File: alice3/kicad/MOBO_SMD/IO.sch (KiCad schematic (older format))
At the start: 36 parts, among them CON1 MicroSD, P2 USB_OTG, P3 UART1, SW2 SOFT RESET, U5 STM32F415RG, Y2 16MHz, Y3 32.768KHz

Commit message: Fix up various small things.
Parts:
- added C?: 1µ, Capacitors_SMD:C_0805, symbol C_Small
- added C?: 4.7µ, Capacitors_SMD:C_0805, symbol C_Small
- added F?: F_Small, symbol F_Small
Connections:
- wire segments 108 -> 148
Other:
- moved on the sheet: C2, C8, JP1, R3, R4

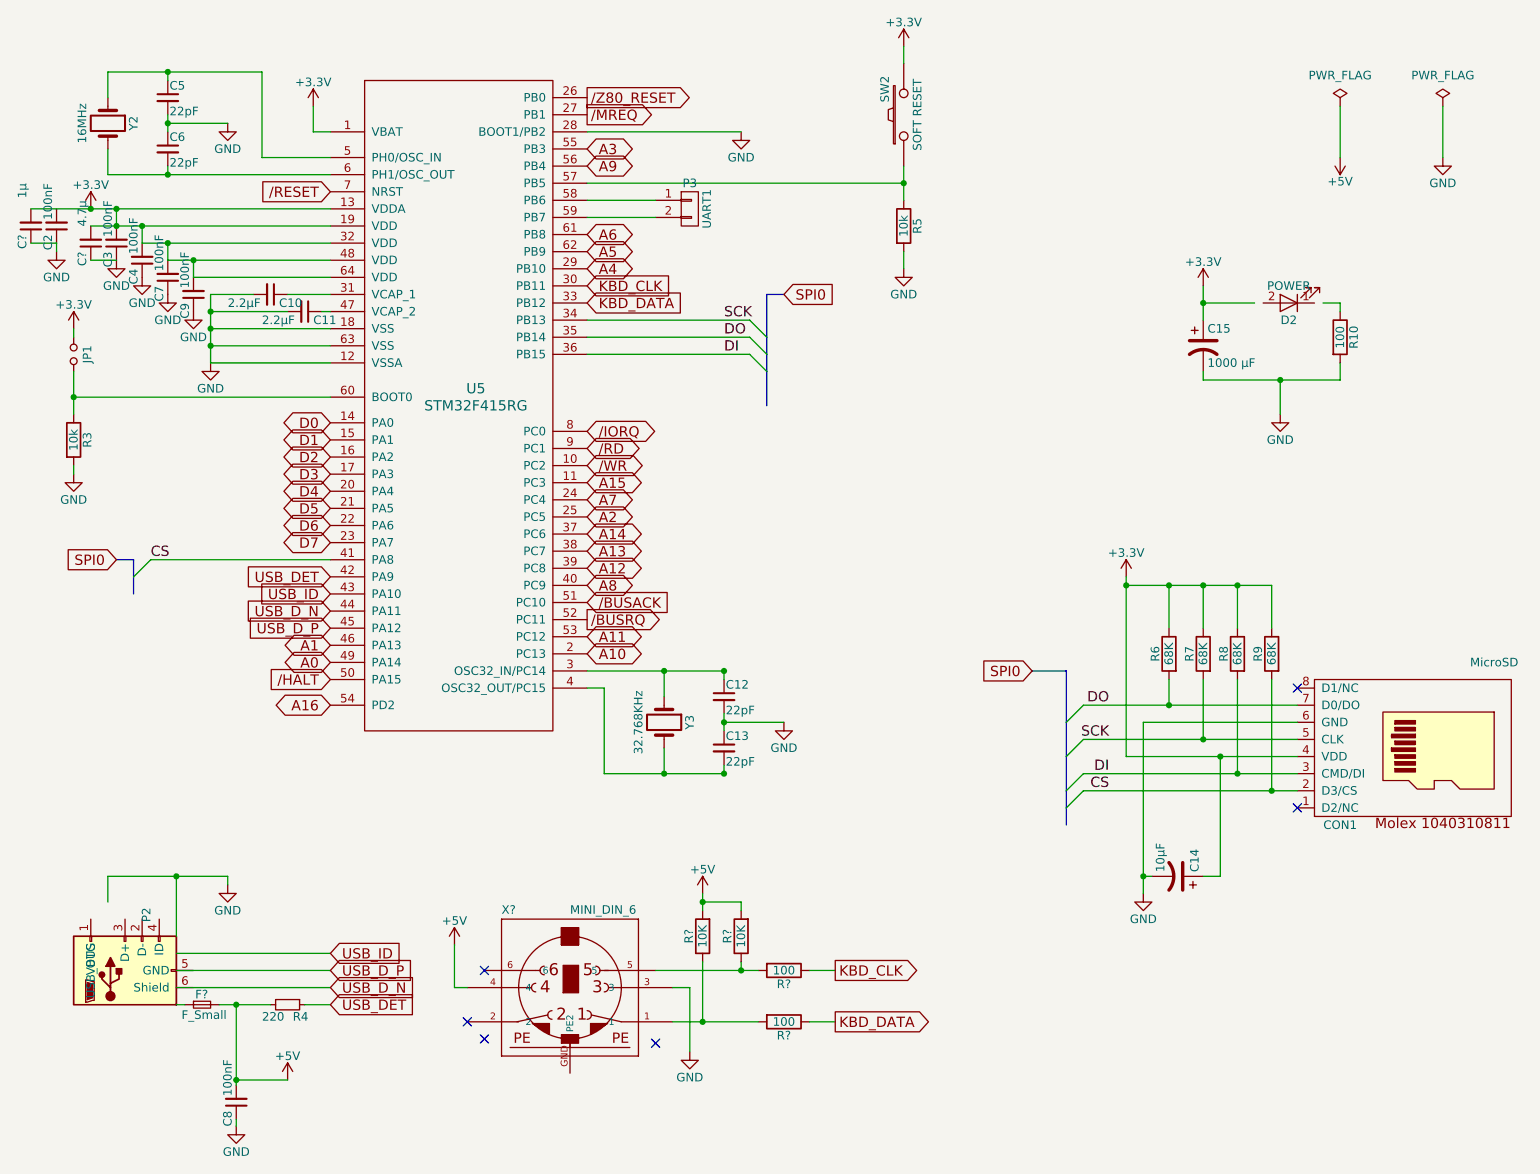
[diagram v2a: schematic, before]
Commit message: Assign part names.
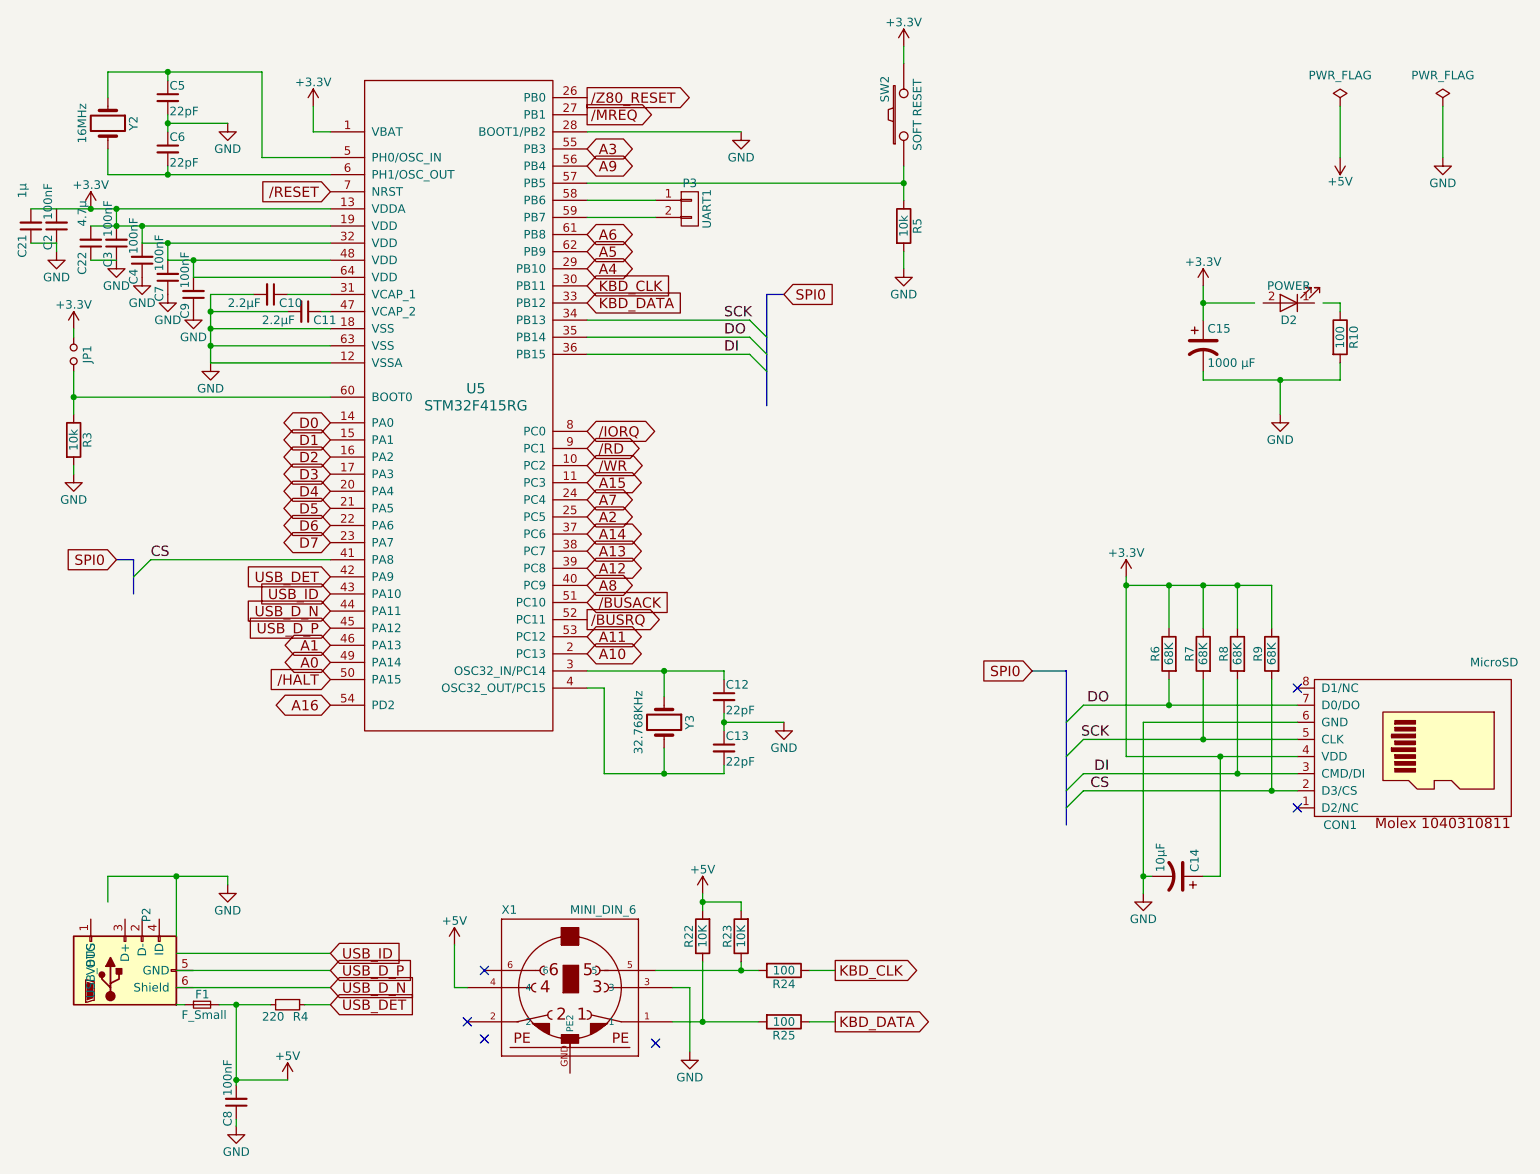
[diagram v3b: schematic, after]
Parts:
- gave numbers to parts that had none: 8
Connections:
- wire segments 148 -> 113

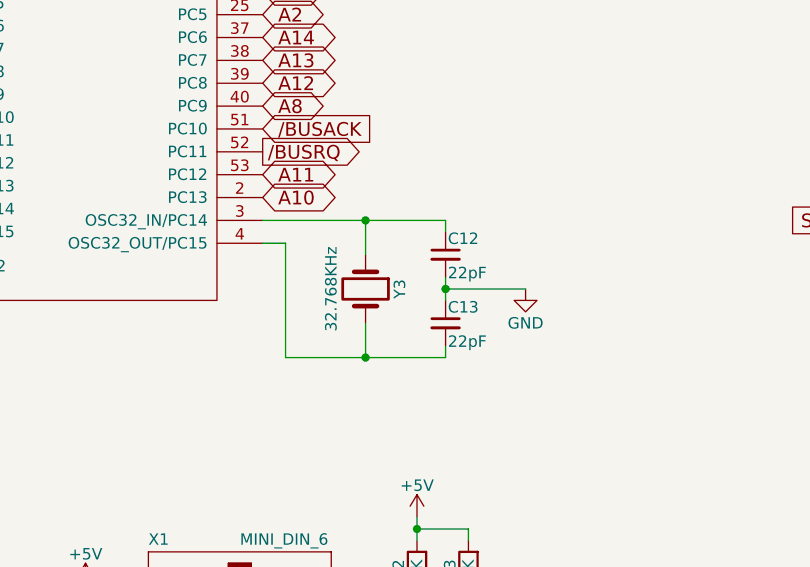
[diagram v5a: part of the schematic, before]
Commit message: Add PROP_READY line; add A17 to ARM.
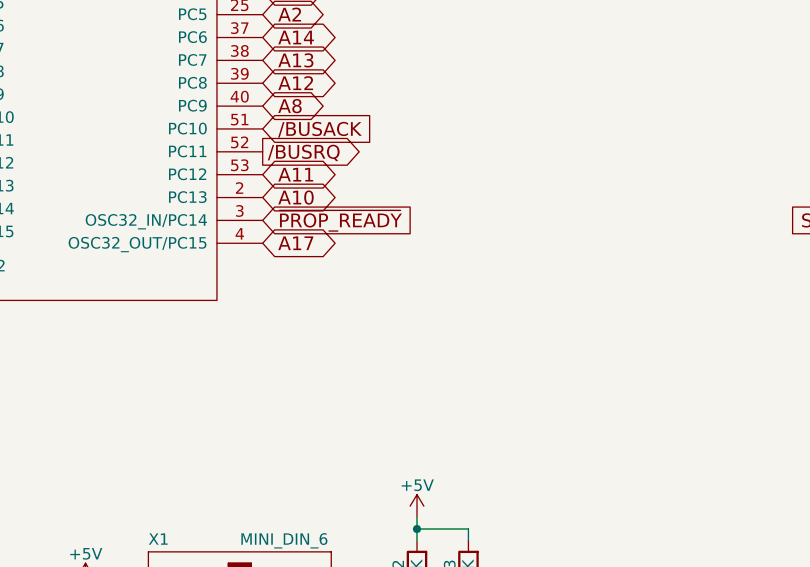
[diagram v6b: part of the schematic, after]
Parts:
- removed C12, C13: 22pF, Capacitors_SMD:C_0805, symbol C_Small
- removed Y3: 32.768KHz, Resistors_SMD:R_0805, symbol Crystal
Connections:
- net labels added: A17, ~PROP_READY~
- wire segments 113 -> 103
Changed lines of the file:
@@
-$EndComp
-$Comp
-L Crystal Y3
-U 1 1 56BA69BE
-P 4350 4900
-F 0 "Y3" H 4350 5050 50  0000 C CNN
-F 1 "32.768KHz" H 4350 4750 50  0000 C CNN
-F 2 "Resistors_SMD:R_0805" H 4350 4900 60  0001 C CNN
-F 3 "" H 4350 4900 60  0000 C CNN
-	1    4350 4900
-	0    1    1    0
-$EndComp
-$Comp
-L GND #PWR32
-U 1 1 56BA69C4
-P 5050 4900
-F 0 "#PWR32" H 5050 4650 50  0001 C CNN
-F 1 "GND" H 5050 4750 50  0000 C CNN
-F 2 "" H 5050 4900 60  0000 C CNN
-F 3 "" H 5050 4900 60  0000 C CNN
-	1    5050 4900
-	1    0    0    -1
-$EndComp
-$Comp
-L C_Small C12
-U 1 1 56BA69CA
-P 4700 4750
-F 0 "C12" H 4710 4820 50  0000 L CNN
-F 1 "22pF" H 4710 4670 50  0000 L CNN
-F 2 "Capacitors_SMD:C_0805" H 4700 4750 60  0001 C CNN
-F 3 "" H 4700 4750 60  0000 C CNN
-	1    4700 4750
-	1    0    0    -1
-$EndComp
-$Comp
-L C_Small C13
-U 1 1 56BA69D0
-P 4700 5050
-F 0 "C13" H 4710 5120 50  0000 L CNN
-F 1 "22pF" H 4710 4970 50  0000 L CNN
-F 2 "Capacitors_SMD:C_0805" H 4700 5050 60  0001 C CNN
-F 3 "" H 4700 5050 60  0000 C CNN
-	1    4700 5050
-	1    0    0    -1
 $EndComp
 $Comp
@@
 Connection ~ 900  3000
 Wire Wire Line
-	4350 4750 4350 4600
-Wire Wire Line
-	4700 4900 5050 4900
-Wire Wire Line
-	4350 5050 4350 5200
-Wire Wire Line
-	4700 4600 4700 4650
-Wire Wire Line
-	4700 4850 4700 4950
-Connection ~ 4700 4900
-Wire Wire Line
-	4700 5200 4700 5150
-Wire Wire Line
-	3900 4600 4700 4600
-Connection ~ 4350 4600
-Wire Wire Line
-	3900 4700 4000 4700
-Wire Wire Line
-	4000 4700 4000 5200
-Wire Wire Line
-	4000 5200 4700 5200
-Connection ~ 4350 5200
-Wire Wire Line
 	6800 5000 8050 5000
 Wire Wire Line
@@
 	1750 6550 2050 6550
 Connection ~ 1850 6550
+Text GLabel 3900 4600 2    60   Input ~ 0
+~PROP_READY~
+Text GLabel 3900 4700 2    60   BiDi ~ 0
+A17
 $EndSCHEMATC
